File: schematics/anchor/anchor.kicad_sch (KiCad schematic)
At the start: 21 parts, among them J1 IEC_60320_C14_Receptacle, J2 120VAC-L, J3 120VAC-N, J4 Earth, M1 Fan_3pin, SW1 SW_DPST, T1 Meanwell_UHP-200-48, T2 Meanwell_UHP-200-24, T3 Meanwell_UHP-200-5, U1 Crydom_D2440_SPST_SSR-NO, U2 Crydom_D2440_SPST_SSR-NO, U3 Crydom_D2440_SPST_SSR-NO, U4 Schneider_Electric_DPE25BL, U5 Crydom_D2440_SPST_SSR-NO

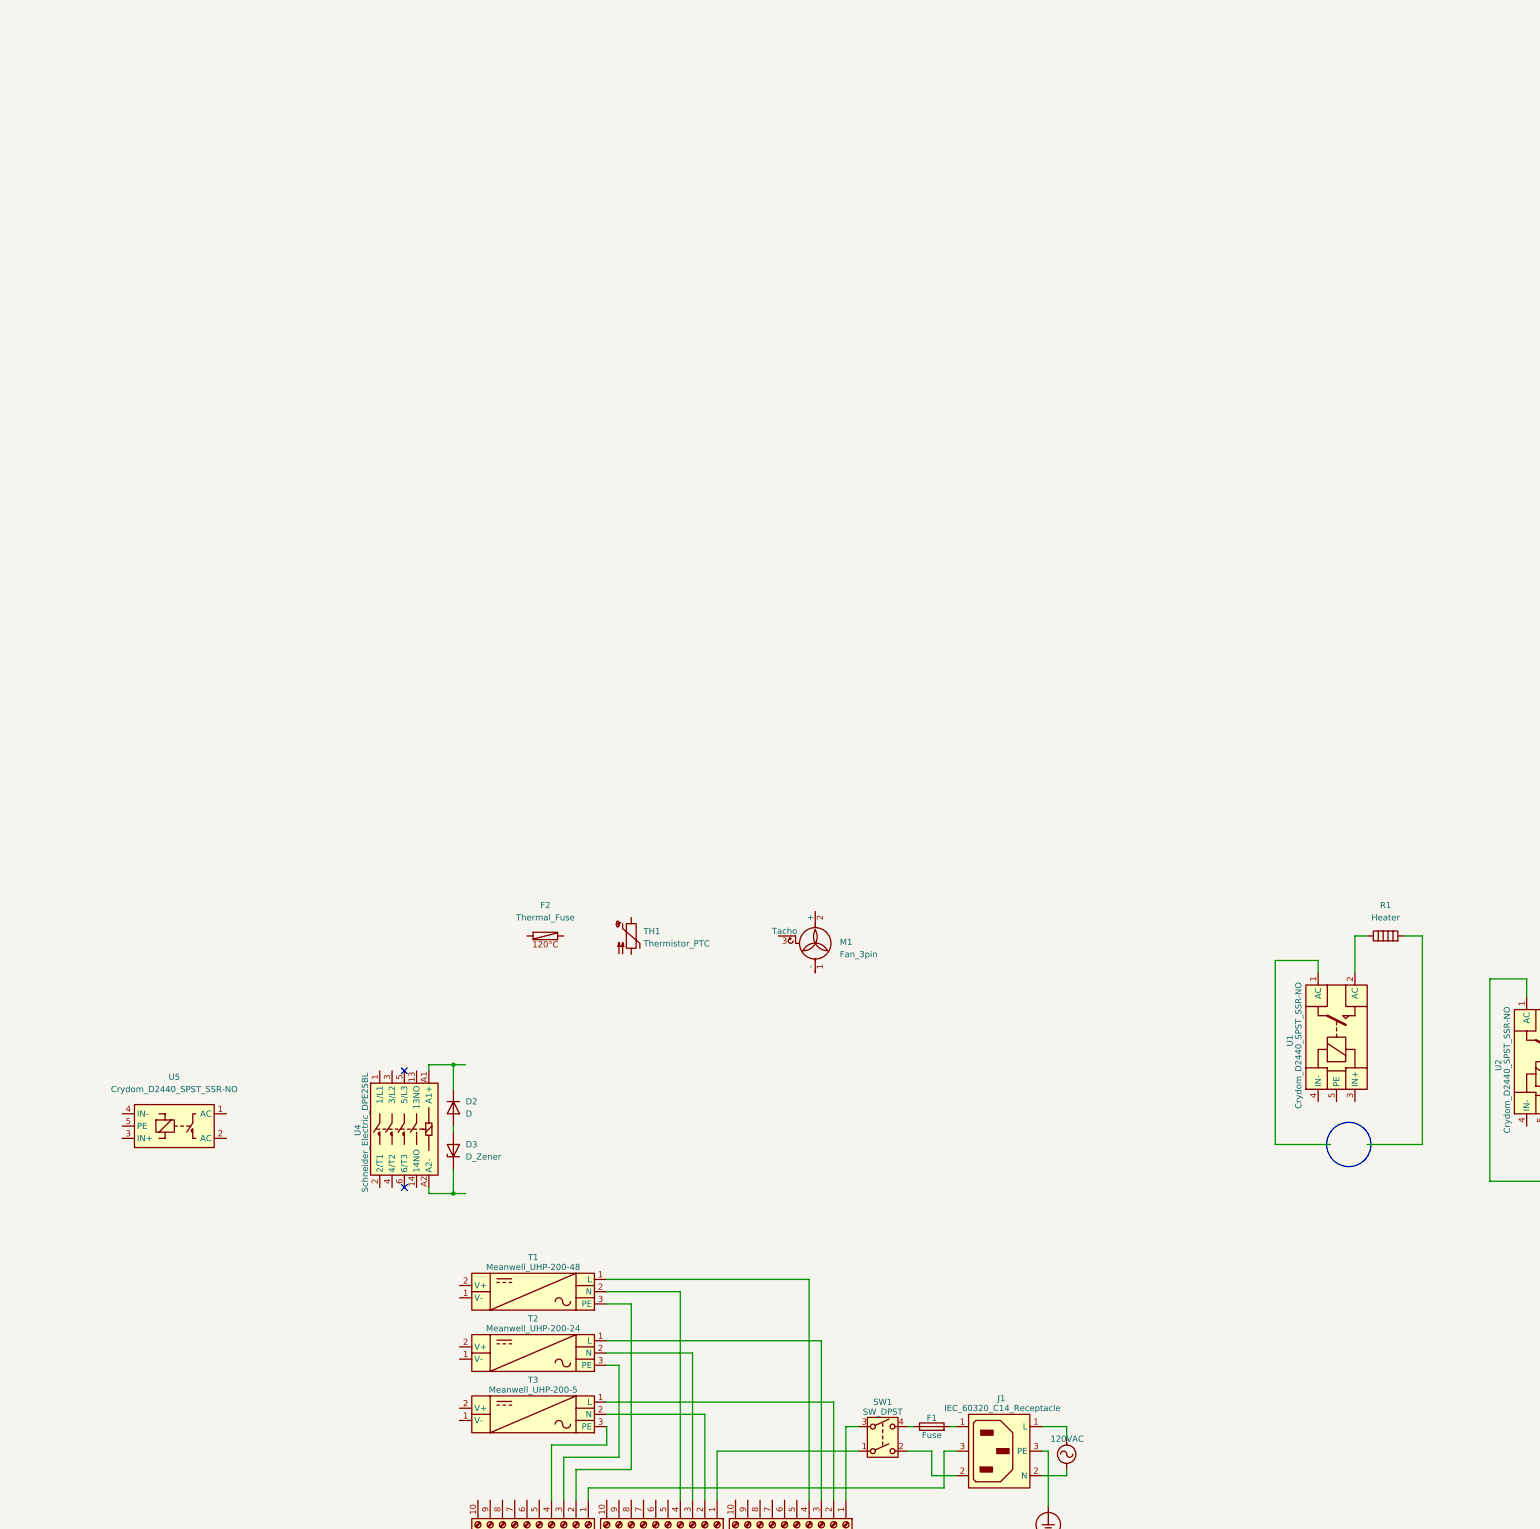
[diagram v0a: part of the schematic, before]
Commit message: Finish bed & chamber heater wiring
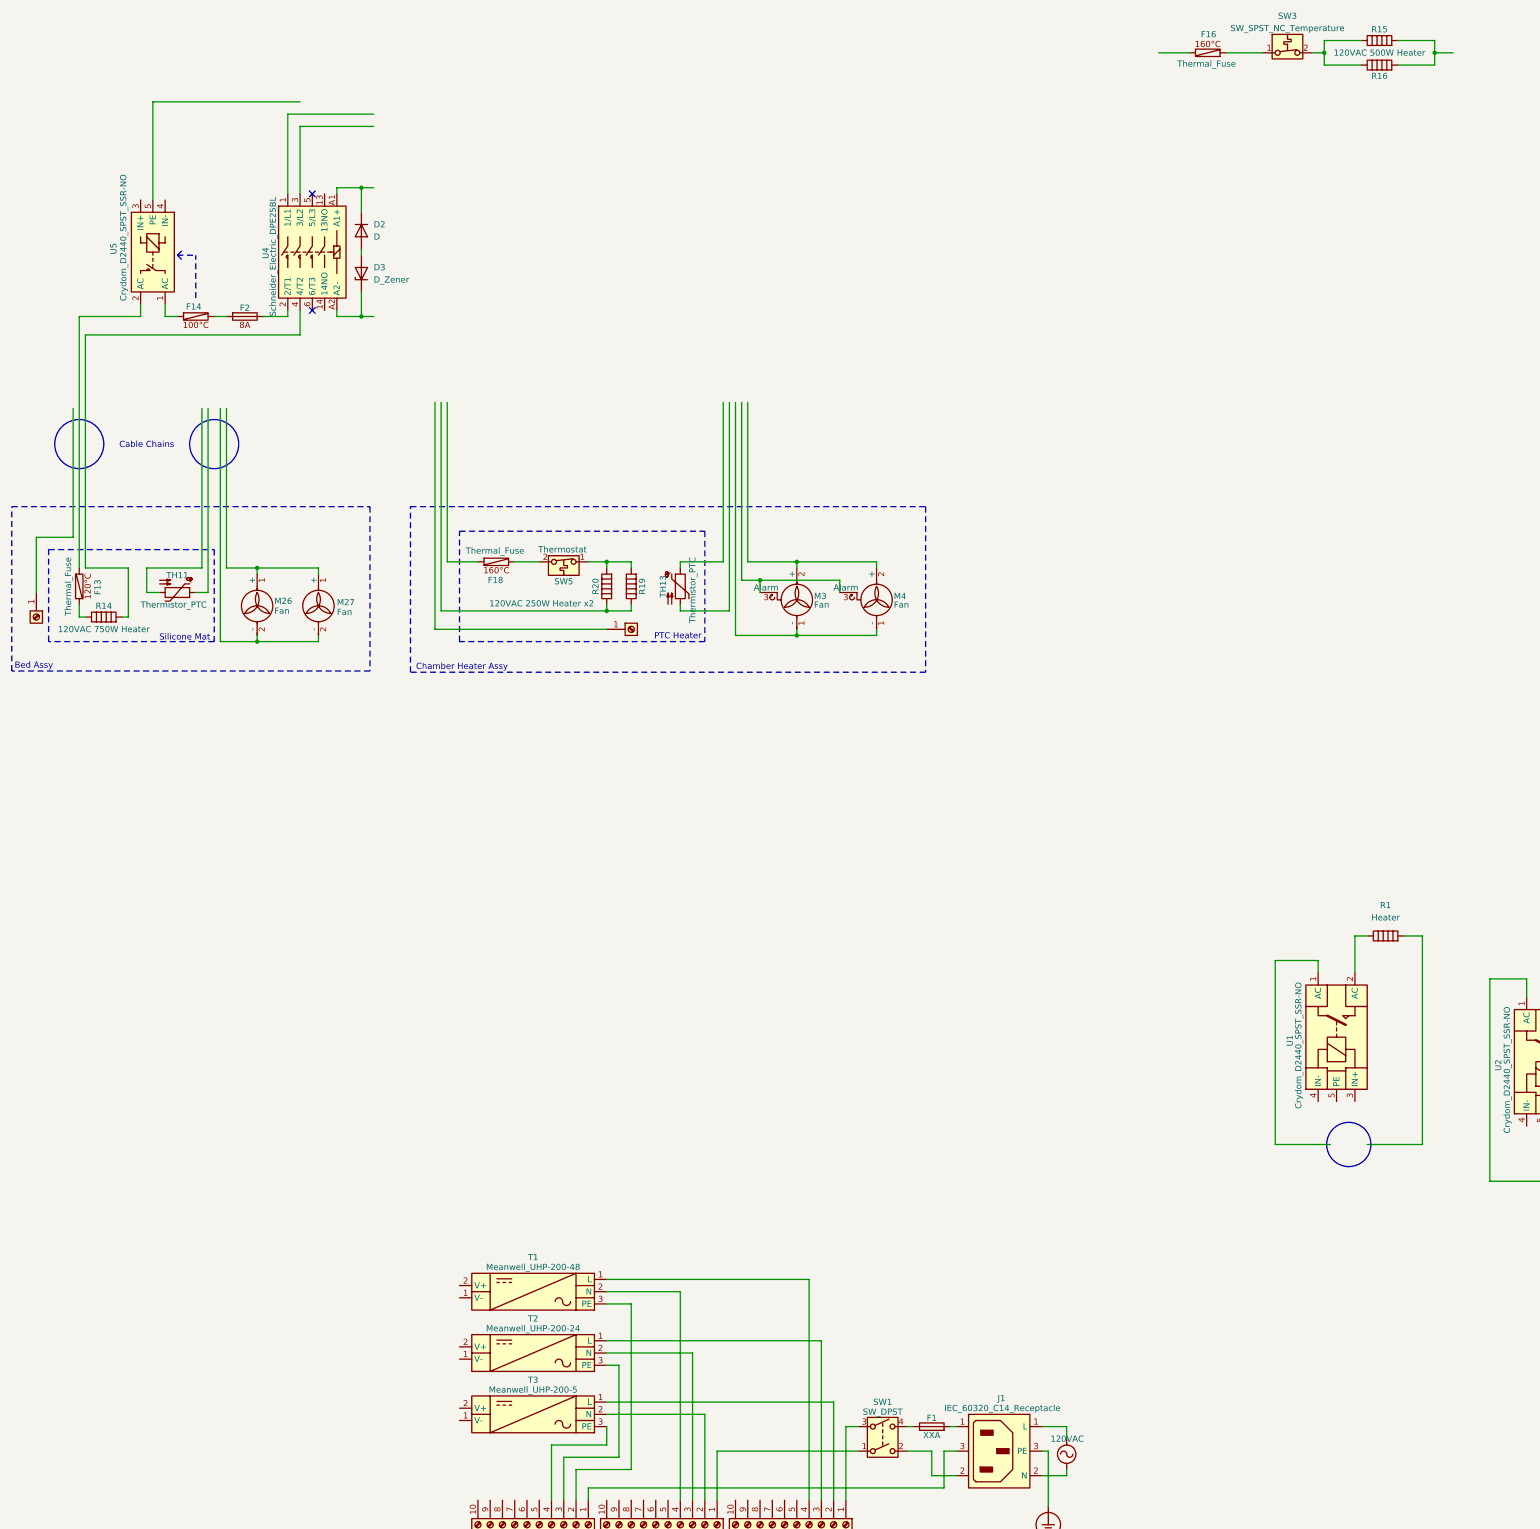
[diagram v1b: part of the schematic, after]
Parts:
- removed F2: Thermal_Fuse, symbol jmatt:Thermal_Fuse
- removed M1: Fan_3pin, symbol Motor:Fan_3pin
- removed TH1: Thermistor_PTC, symbol Device:Thermistor_PTC
- added F13, F14, F16, F18: Thermal_Fuse, symbol jmatt:Thermal_Fuse
- added F2: Fuse, symbol Device:Fuse
- added J16, J18: Screw_Terminal_01x01, symbol Connector:Screw_Terminal_01x01
- added M26, M27: Fan, symbol Motor:Fan
- added M3, M4: Fan, symbol Motor:Fan_3pin
- added R14: 120VAC 750W Heater, symbol Device:Heater
- added R15, R16, R19: 120VAC 500W Heater, symbol Device:Heater
- added R20: 120VAC 250W Heater x2, symbol Device:Heater
- added SW3: SW_SPST_NC_Temperature, symbol jmatt:SW_SPST_NC_Temperature
- added SW5: Thermostat, symbol jmatt:SW_SPST_NC_Temperature
- added TH11, TH13: Thermistor_PTC, symbol Device:Thermistor_PTC
- F1: value Fuse -> XXA
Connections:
- net at U4.2 (2/T1): now also F2.1
- net at U4.4 (4/T2): now also R14.2
- net at J1.1 (L): now also F1.2
- net at U5.1 (AC): now also F14.2
- net at U5.2 (AC): now also F13.1
- new net: F18.1, SW5.2 (B)
- new net: M26.1 (+), M27.1 (+)
- new net: M26.2 (-), M27.2 (-)
- new net: R15.1, R16.1, SW3.2 (B)
- new net: R15.2, R16.2
- new net: R19.1, R20.1
- new net: R19.2, R20.2, SW5.1 (A)
- new net: F16.2, SW3.1 (A)
- new net: F13.2, R14.1
- new net: F14.1, F2.2
- new net: M3.1 (-), M4.1 (-)
- new net: M3.2 (+), M4.2 (+)
- new net: M3.3 (Alarm), M4.3 (Alarm)
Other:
- note added: "Bed Assy"
- note added: "Cable Chains"
- note added: "Chamber Heater Assy"
- note added: "PTC Heater"
- note added: "Silicone Mat"
- moved on the sheet: D2, D3, U4, U5

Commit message: Start DFMEA study
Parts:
- removed F16: Thermal_Fuse, symbol jmatt:Thermal_Fuse
- removed R15, R16: 120VAC 500W Heater, symbol Device:Heater
- removed SW3: SW_SPST_NC_Temperature, symbol jmatt:SW_SPST_NC_Temperature
- added D4: D, symbol Device:D
- added D5: D_Zener, symbol Device:D_Zener
- added F15: Thermal_Fuse, symbol jmatt:Thermal_Fuse
- added F3: Fuse, symbol Device:Fuse
- added U6: Crydom_D2440_SPST_SSR-NO, symbol jmatt:Crydom_D2440_SPST_SSR-NO
- added U7: Schneider_Electric_DPE25BL, symbol jmatt:Schneider_Electric_DPE25BL
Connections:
- net at F18.2: now also U6.2 (AC)
- net at R19.1, R20.1: now also U7.4 (4/T2)
- net at J1.1 (L): now also F1.2
- new net: D5.1 (K), U7.A2 (A2-)
- new net: D4.2 (A), D5.2 (A)
- new net: F3.1, U7.2 (2/T1)
- new net: D4.1 (K), U7.A1 (A1+)
- new net: F15.2, U6.1 (AC)
- new net: F15.1, F3.2
- no-connect marks 2 -> 4
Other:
- company: (none) -> jmatt
- title: (none) -> Anchor
- moved on the sheet: F1, F18, J1, J2, J3, J4, M3, M4, R19, R20, SW1, SW5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

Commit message: Add raspberry pi-controlled relay circuit
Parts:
- removed F1: XXA, symbol Device:Fuse
- removed J1: IEC_60320_C14_Receptacle, symbol Connector:IEC_60320_C14_Receptacle
- removed J2: 120VAC-L, symbol Connector:Screw_Terminal_01x10
- removed J3: 120VAC-N, symbol Connector:Screw_Terminal_01x10
- removed J4: Earth, symbol Connector:Screw_Terminal_01x10
- removed R1, R2: Heater, symbol Device:Heater
- removed SW1: SW_DPST, symbol Switch:SW_DPST
- removed T3: Meanwell_UHP-200-5, symbol jmatt:UHP-200-24
- removed U1, U2, U3: Crydom_D2440_SPST_SSR-NO, symbol jmatt:Crydom_D2440_SPST_SSR-NO
- added F16: Thermal_Fuse, symbol jmatt:Thermal_Fuse
- added F4: Fuse, symbol Device:Fuse
- added F5: XXA, symbol Device:Fuse
- added J7: IEC_60320_C14_Receptacle, symbol Connector:IEC_60320_C14_Receptacle
- added R15, R17, R18: 24VDC 100W Heater, symbol Device:Heater
- added SW2: SW_DPST, symbol Switch:SW_DPST
- added T5: Meanwell_UHP-200-5, symbol jmatt:UHP-200-24
- added TH14, TH16, TH17: Thermistor_PTC, symbol Device:Thermistor_PTC
- added U1, U11, U2, U3, U9: Phoenix_Contact_PTFIX_6x2, symbol jmatt:Phoenix_Contact_PTFIX_6x2
- added U10: Beacon_Regulator, symbol jmatt:Beacon_Regulator
- added U13: Phoenix_Contact_PTFIX_12x2, symbol jmatt:Phoenix_Contact_PTFIX_12x2
- added U22: Schneider_Electric_DPE25G7, symbol jmatt:Schneider_Electric_DPE25G7
- added U23: Raspberry_Pi, symbol jmatt:Raspberry_Pi
- added U24: Adafruit_Feather_Relay, symbol jmatt:Adafruit_Feather_Relay
- added U8: Beacon_Eddy_Scanner, symbol jmatt:Beacon_Eddy_Scanner
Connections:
- net Earth_Protective: now also J7.3 (PE)
- net at T1.3 (PE): now also U13.10
- net at T2.3 (PE): now also U13.11
- net at T2.1 (V-): now also U9.5
- net at T1.1 (V-): now also U9.4
- new net: U1.1, U22.1 (1/L1)
- new net: U22.2 (2/T1), U9.6
- new net: U2.1, U22.3 (3/L2)
- new net: U22.4 (4/T2), U3.6
- new net: U22.A1, U24.
- new net: U2.4, U22.A2
- new net: T1.2 (V+), U3.4
- new net: T2.2 (V+), U3.5
- new net: T5.2 (V+), U2.2
- new net: SW2.1, U2.3
- new net: U11.4, U13.12
- new net: F5.1, SW2.4
- new net: F5.2, J7.1 (L)
- new net: T5.3 (PE), U11.2
- new net: J7.3 (PE), U11.6
- new net: U10.5, U23. (+5VDC)
- new net: U10.6, U23. (+5VDC)
- new net: U10.7, U23. (+5VDC)
- new net: U10.8, U23. (+5VDC)
- new net: J7.2 (N), SW2.2
- new net: T5.1 (V-), U1.2
- new net: SW2.3, U1.3
- new net: U1.4, U24.
- new net: T5.1 (V-), U23. (+5VDC), U24.4 (GND)
- new net: T5.2 (V+), U23. (+5VDC), U24.2 (+5VDC)
- new net: U23.16 (GPIO23), U24.5 (RELAY)
- no-connect marks 4 -> 16
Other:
- note added: "//TODO"
- moved on the sheet: T1, T2, TH11

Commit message: Clean up schematic
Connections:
- net at U3.2: now also U4.3 (3/L2)
- net at U3.3: now also U7.3 (3/L2)
- net at U13.5: now also U5.5 (PE)
- net at U13.6: now also U6.5 (PE)
- net at U13.8: now also J16.1 (Pin_1)
- net at U13.9: now also J18.1 (Pin_1)
- net at U7.1 (1/L1): now also U9.3
- net at U4.1 (1/L1): now also U9.2
- net at J7.2 (N): now also SW2.2
- net at T1.1 (V-): now also U9.4
- net at T2.1 (V-): now also U9.5
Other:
- note added: "Toolhead Assy"
- moved on the sheet: D2, D3, D4, D5, F13, F14, F15, F16, F18, F2, F3, F4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

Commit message: Add better contactors snubbers
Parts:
- removed D2, D4: D, symbol Device:D
- removed D3, D5: D_Zener, symbol Device:D_Zener
- removed F16: Thermal_Fuse, symbol jmatt:Thermal_Fuse
- removed R18: 24VDC 100W Heater, symbol Device:Heater
- removed TH17: Thermistor_PTC, symbol Device:Thermistor_PTC
- added D8: D, symbol Device:D
- added D9: D_Zener, symbol Device:D_Zener
- added M1: Motor_X0, symbol Motor:Stepper_Motor_bipolar
- added M10: Motor_Z2, symbol Motor:Stepper_Motor_bipolar
- added M2: Motor_Y0, symbol Motor:Stepper_Motor_bipolar
- added M5: Motor_X1, symbol Motor:Stepper_Motor_bipolar
- added M6: Motor_Y1, symbol Motor:Stepper_Motor_bipolar
- added M7: Motor_E0, symbol Motor:Stepper_Motor_bipolar
- added M8: Motor_Z0, symbol Motor:Stepper_Motor_bipolar
- added M9: Motor_Z1, symbol Motor:Stepper_Motor_bipolar
- added U12, U14: Schneider_Electric_DPE25BL, symbol jmatt:Schneider_Electric_DPE25BL
- added U15, U16, U17: ~, symbol jmatt:Murrelektronik_Diode_Zener_Suppressor
- added U18: ~, symbol jmatt:Murrelektronik_26183_Varistor_Suppressor
- added U19: BTT_TMC5160T_Plus, symbol jmatt:BTT_TMC5160T_Plus
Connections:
- net at U4.A2 (A2-): now also U15.2 (-)
- net at U4.A1 (A1+): now also U15.1 (+)
- net at U22.A1, U24.: now also U18.1
- net at U2.4, U22.A2: now also U18.2
- net at U7.A2 (A2-): now also U17.2 (-)
- net at R15.1: now also F4.2
- net at R15.2: now also U12.4 (4/T2)
- net at U7.A1 (A1+): now also U17.1 (+)
- net at J7.2 (N): now also SW2.2
- net at T1.1 (V-): now also U9.4
- net at F4.1: now also U12.2 (2/T1)
- net at T2.1 (V-): now also U9.5
- new net: M1.2 (-), U19.1 (B1)
- new net: M1.1, U19.2 (B2)
- new net: M1.3, U19.3 (A1)
- new net: M1.4, U19.4 (A2)
- new net: D9.1 (K), U14.A2 (A2-)
- new net: D8.2 (A), D9.2 (A)
- new net: D8.1 (K), U14.A1 (A1+)
- new net: U12.A1 (A1+), U16.1 (+)
- new net: U12.A2 (A2-), U16.2 (-)
- new net 48VDC: U19.6 (+)
- new net GND: U19.5 (-)
- no-connect marks 16 -> 20
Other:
- moved on the sheet: F13, F4, M26, M27, R14, TH11, U22, U23, U24, U8
